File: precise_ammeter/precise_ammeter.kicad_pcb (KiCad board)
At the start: 2 copper layers, 104 parts, among them J1 Conn_01x01_Socket, J2 Conn_01x01_Socket, J3 USB4110GFA, J4 Conn_ARM_JTAG_SWD_10, J5 XT30_Male, J6 Conn_01x04_Socket, U1 INA121U, U10 TPS7A2450DBVR, U11 STM32G431C6Tx, U12 USBLC6-2P6, U2 TLV9301xDBV, U3 TLV9301xDBV, U4 INA137UA, U5 OPA376xxD, U6 OPA376xxD, U7 TPS7A2433DBVR, U8 TPS7A2450DBVR, U9 LMC7660, Y1 Crystal 8MHz

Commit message: layout started
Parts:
- U10, U8: footprint TPS7A2450DBVR:SOT_50DBVR -> TPS7A2433DBVR:SOT23_DBV_TEX
- moved C32 125.6 mm to (233.8, 85.8)
- moved C34 124.4 mm to (235.1, 77.2), turned to 90 degrees
- moved C37 121.1 mm to (231.8, 89.0)
- moved C35 119.6 mm to (228.2, 89.2), turned to 180 degrees
- moved C36 117.9 mm to (228.2, 87.1), turned to 180 degrees
- moved C33 114.5 mm to (225.1, 74.5), turned to 180 degrees
- moved C30 113.9 mm to (222.3, 77.2), turned to 90 degrees
- moved C38 107.2 mm to (216.4, 94.2)
- moved C29 102.2 mm to (213.7, 48.4)
- moved C31 102.2 mm to (213.7, 54.5)
- moved D3 102.2 mm to (237.5, 63.6)
- moved Y1 102.2 mm to (232.5, 50.3)
- moved D4 102.2 mm to (227.9, 55.4)
- moved D5 102.2 mm to (227.9, 58.7)
- moved D6 102.2 mm to (227.9, 62.0)
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
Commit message: USB layout
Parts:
- moved J3 136.7 mm to (246.4, 78.3), turned to 90 degrees
- moved Y1 41.1 mm to (212.1, 86.0), turned to -90 degrees
- moved C31 35.4 mm to (216.1, 89.8), turned to -90 degrees
- moved C29 32.4 mm to (216.0, 80.8), turned to 90 degrees
- moved R25 32.3 mm to (216.1, 86.0), turned to 90 degrees
- moved D4 20.3 mm to (208.1, 50.8)
- moved D5 20.3 mm to (208.1, 54.1)
- moved D7 20.3 mm to (208.1, 60.8)
- moved D6 20.3 mm to (208.1, 57.5)
- moved C38 19.0 mm to (222.3, 76.2), turned to 90 degrees
- moved D3 14.9 mm to (227.0, 53.0)
- moved U12 13.4 mm to (236.7, 78.3)
- moved R1 12.5 mm to (226.3, 60.4)
- moved R5 11.8 mm to (230.4, 60.4)
- moved C37 5.31 mm to (235.7, 85.3), turned to -90 degrees
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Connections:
- U12 pad 1: Net-(U11-PA11) -> Net-(U11-PA12)
- U12 pad 3: Net-(U11-PA12) -> Net-(U11-PA11)
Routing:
- net /MCU/USB_D_N: track 0.00 -> 11.3 mm
- net /MCU/USB_D_P: track 0.00 -> 7.93 mm
- net Net-(U11-PA11): track 0.00 -> 2.81 mm
- net Net-(U11-PA12): track 0.00 -> 2.81 mm

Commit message: idk
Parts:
- moved R28 138.7 mm to (244.8, 72.8), turned to 90 degrees
- moved R29 138.4 mm to (244.8, 84.3), turned to -90 degrees
- moved J5 119.7 mm to (236.5, 94.4)
- moved J6 79.7 mm to (234.0, 65.1), turned to 90 degrees
- moved C1 63.3 mm to (191.2, 77.1)
- moved C5 63.3 mm to (191.2, 80.1)
- moved U7 63.3 mm to (185.9, 78.0)
- moved D6 33.9 mm to (213.0, 91.0)
- moved D7 33.9 mm to (213.0, 94.3)
- moved D5 33.9 mm to (213.0, 87.6)
- moved D4 29.5 mm to (215.4, 79.3), turned to -90 degrees
- moved C31 19.3 mm to (205.6, 73.5), turned to 180 degrees
- moved Y1 16.9 mm to (208.7, 69.4), turned to 180 degrees
- moved D3 15.2 mm to (227.3, 68.2), turned to 90 degrees
- moved R25 13.8 mm to (208.5, 74.4)
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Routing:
- net /MCU/USB_D_P: track 7.93 -> 13.6 mm, vias 0 -> 2
- net Net-(J3-CC2): track 0.00 -> 5.03 mm
- net GND: track 0.00 -> 2.62 mm, vias 0 -> 2
- net /MCU/USB_D_N: track 11.3 -> 13.5 mm
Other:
- board text added: "GND"
- board text added: "SCL"
- board text added: "SDA"
- board text added: "VCC"

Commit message: placement finished
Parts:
- moved R14 100.1 mm to (206.3, 96.7), turned to 90 degrees
- moved R15 96.6 mm to (202.9, 91.7), turned to 180 degrees
- moved R17 95.8 mm to (202.1, 101.7), turned to 90 degrees
- moved C40 93.3 mm to (232.4, 63.4)
- moved D4 91.9 mm to (130.5, 44.0)
- moved D5 91.9 mm to (128.1, 52.3)
- moved D6 91.9 mm to (128.1, 55.6)
- moved D7 91.9 mm to (128.1, 59.0)
- moved C13 90.5 mm to (206.3, 92.3), turned to 90 degrees
- moved C14 87.1 mm to (202.9, 98.1)
- moved C12 84.0 mm to (199.8, 93.3), turned to 90 degrees
- moved C16 82.5 mm to (198.2, 100.6), turned to 90 degrees
- moved R20 82.4 mm to (187.8, 94.5), turned to 90 degrees
- moved R21 80.7 mm to (191.7, 94.6), turned to 90 degrees
- moved R30 80.5 mm to (224.6, 66.5)
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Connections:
- J5 pad 1: VBUS -> GND
- J5 pad 2: GND -> VBUS
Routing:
- net Net-(C31-Pad1): track 0.00 -> 6.98 mm
- net +3V3: track 0.00 -> 5.06 mm
- net Net-(U2--): track 0.00 -> 5.06 mm
- net Net-(U4-IN-): track 0.00 -> 2.84 mm
- net /Curr_measurement/Frontend_2/Stage1_out_2: track 0.00 -> 1.27 mm
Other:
- board text added: "CLK"
- board text added: "DIO"
- board text added: "NRST"
- board text added: "OLED"
- board text added: "SWD"

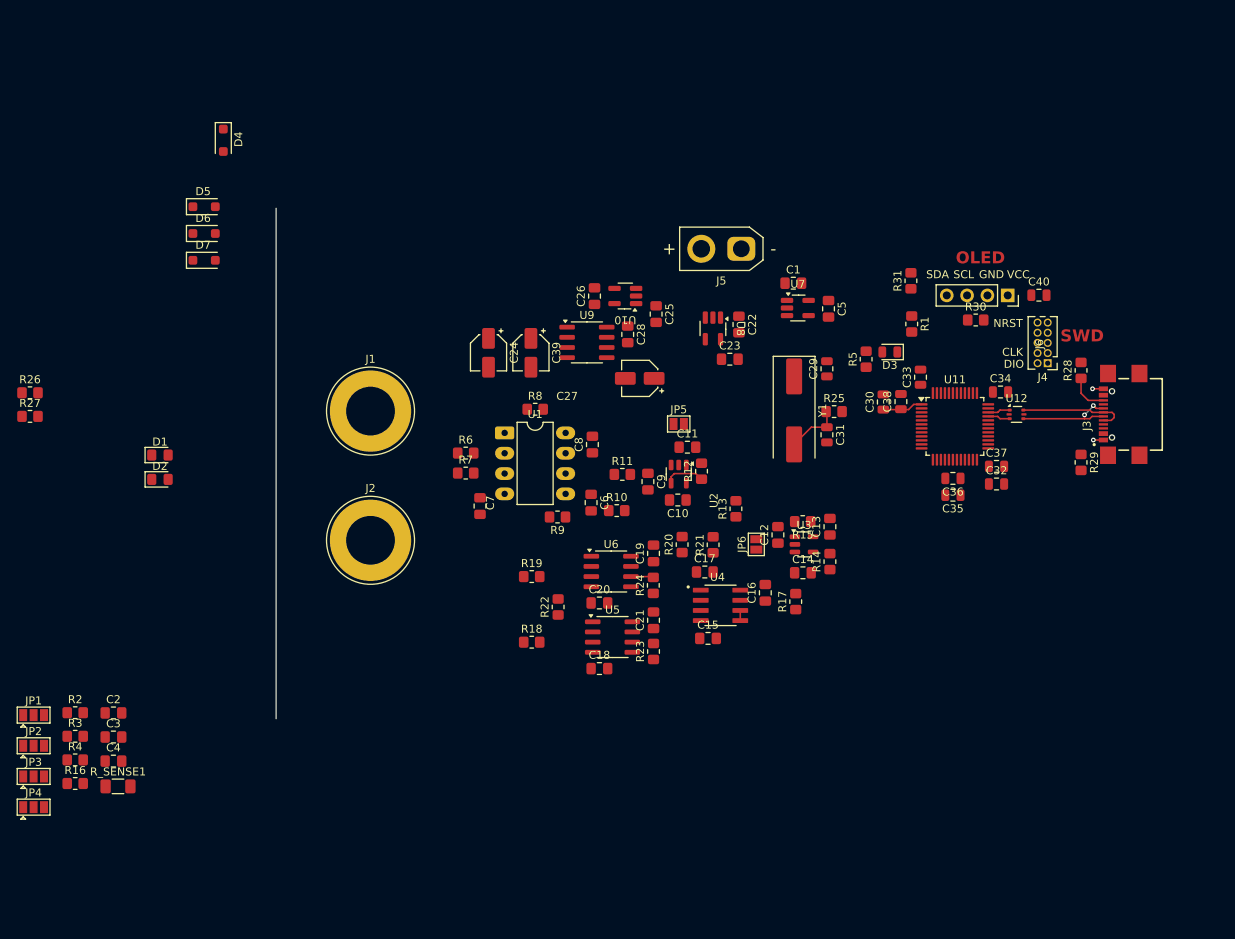
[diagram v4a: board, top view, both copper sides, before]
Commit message: placement changed
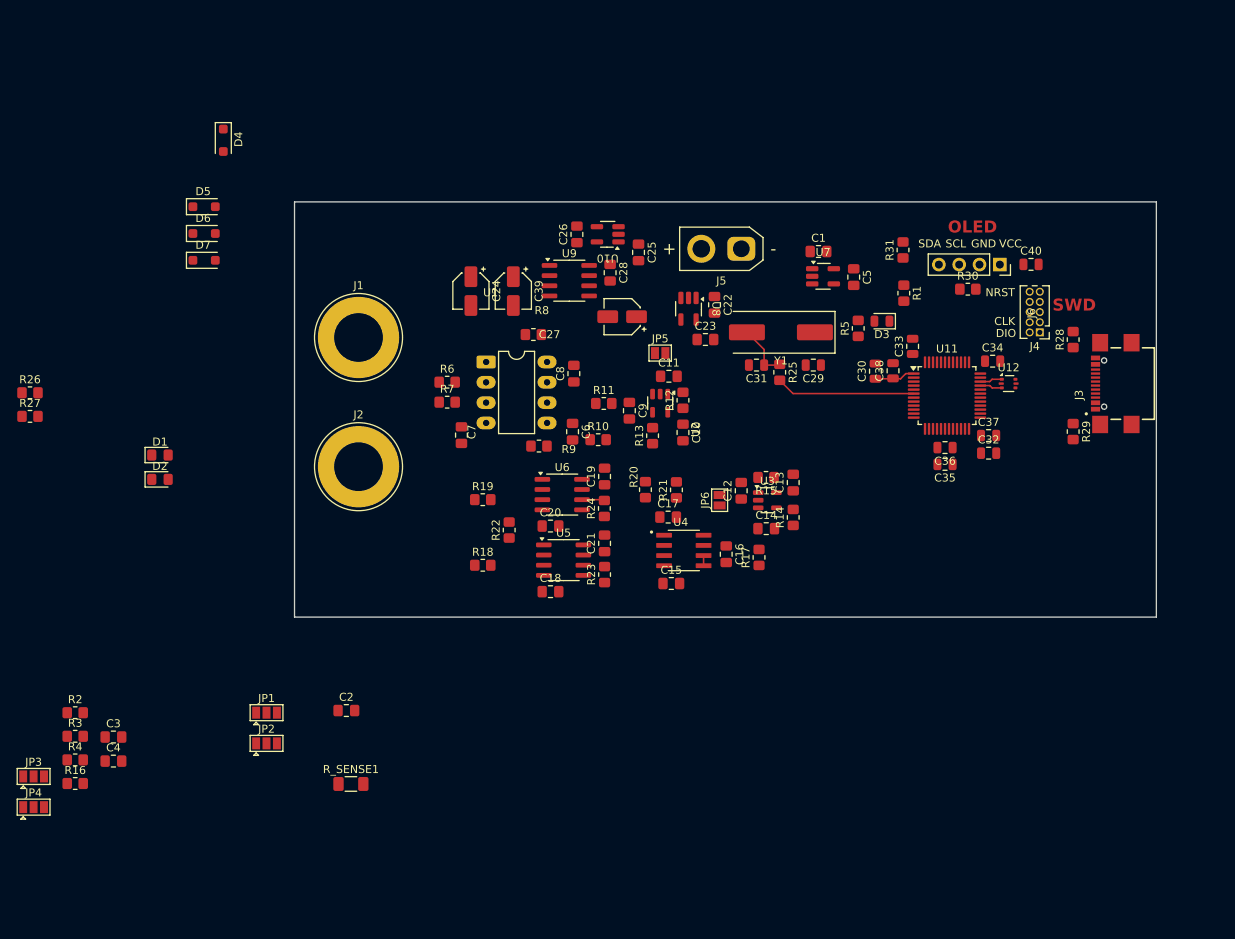
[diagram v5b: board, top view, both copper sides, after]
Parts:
- moved JP1 29.1 mm to (135.9, 115.5)
- moved JP2 29.1 mm to (135.9, 119.4)
- moved C2 29.1 mm to (145.9, 115.3)
- moved R_SENSE1 29.1 mm to (146.4, 124.5)
- moved R13 13.9 mm to (184.2, 80.9)
- moved C31 12.4 mm to (197.2, 72.1), turned to 180 degrees
- moved C19 11.4 mm to (178.2, 86.0)
- moved C21 11.4 mm to (178.2, 94.4)
- moved R24 11.4 mm to (178.1, 90.0)
- moved U6 11.4 mm to (172.9, 88.3)
- moved R18 11.4 mm to (162.9, 97.1)
- moved R19 11.4 mm to (162.9, 88.9)
- moved R22 11.4 mm to (166.2, 92.7)
- moved R23 11.4 mm to (178.2, 98.3)
- moved U5 11.4 mm to (173.0, 96.5)
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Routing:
- net Net-(U11-PF1): track 0.00 -> 17.4 mm
- net /MCU/USB_D_P: track 13.6 -> 0.00 mm, vias 2 -> 0
- net /MCU/USB_D_N: track 13.5 -> 0.00 mm
- net Net-(U2--): track 5.06 -> 0.00 mm
- net Net-(J3-CC2): track 5.03 -> 0.00 mm
- net GND: track 2.62 -> 0.00 mm, vias 2 -> 0
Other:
- board outline added: 107.7 x 51.9 mm

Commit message: jebane gowno
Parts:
- removed C39: 10u, Capacitor_SMD:CP_Elec_4x5.4
- moved R18 91.7 mm to (253.7, 110.3), turned to 90 degrees
- moved JP1 68.1 mm to (201.4, 134.0), turned to 90 degrees
- moved C7 63.1 mm to (216.0, 110.5), turned to 0 degrees
- moved R19 61.7 mm to (205.1, 134.0), turned to 90 degrees
- moved JP3 61.2 mm to (165.2, 105.4)
- moved C13 61.0 mm to (166.9, 136.9), turned to -90 degrees
- moved R14 60.6 mm to (163.4, 138.1)
- moved C19 60.5 mm to (143.1, 135.3)
- moved JP5 60.2 mm to (237.2, 100.7)
- moved C20 59.9 mm to (136.8, 141.1)
- moved R12 59.1 mm to (239.1, 106.2)
- moved R10 59.0 mm to (229.2, 109.7)
- moved C6 59.0 mm to (226.0, 108.7)
- moved R13 59.0 mm to (235.1, 110.7)
- moved C11 59.0 mm to (237.1, 103.2)
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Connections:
- net /Curr_measurement/Analog_out renamed /Analog_IO
- net /Curr_measurement/Stage_1_out renamed /Stage_IO
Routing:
- net Net-(U11-PF1): track 17.4 -> 0.00 mm
- net Net-(C31-Pad1): track 6.98 -> 0.00 mm
- net +3V3: track 5.06 -> 0.00 mm
- net -5VA: track 0.00 -> 3.43 mm
- net Net-(U4-IN-): track 2.84 -> 0.00 mm
- net /Curr_measurement/Frontend_2/Stage1_out_2: track 1.27 -> 0.00 mm
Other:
- board size 107.7 x 51.9 mm -> 71.1 x 73.3 mm
- board text removed: "OLED"

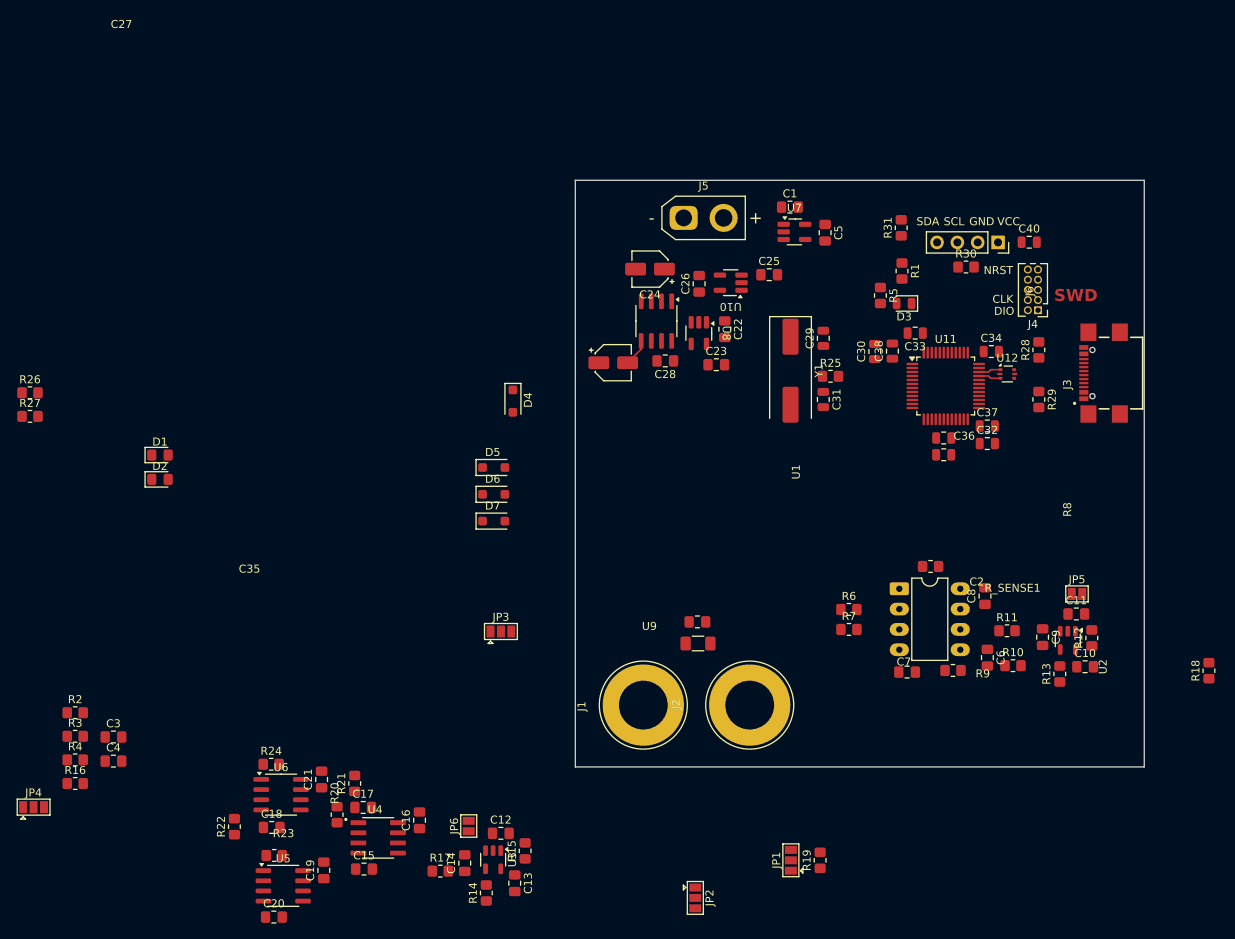
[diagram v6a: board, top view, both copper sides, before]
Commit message: layout almost done. Need to connect Curr_in and fix warnings
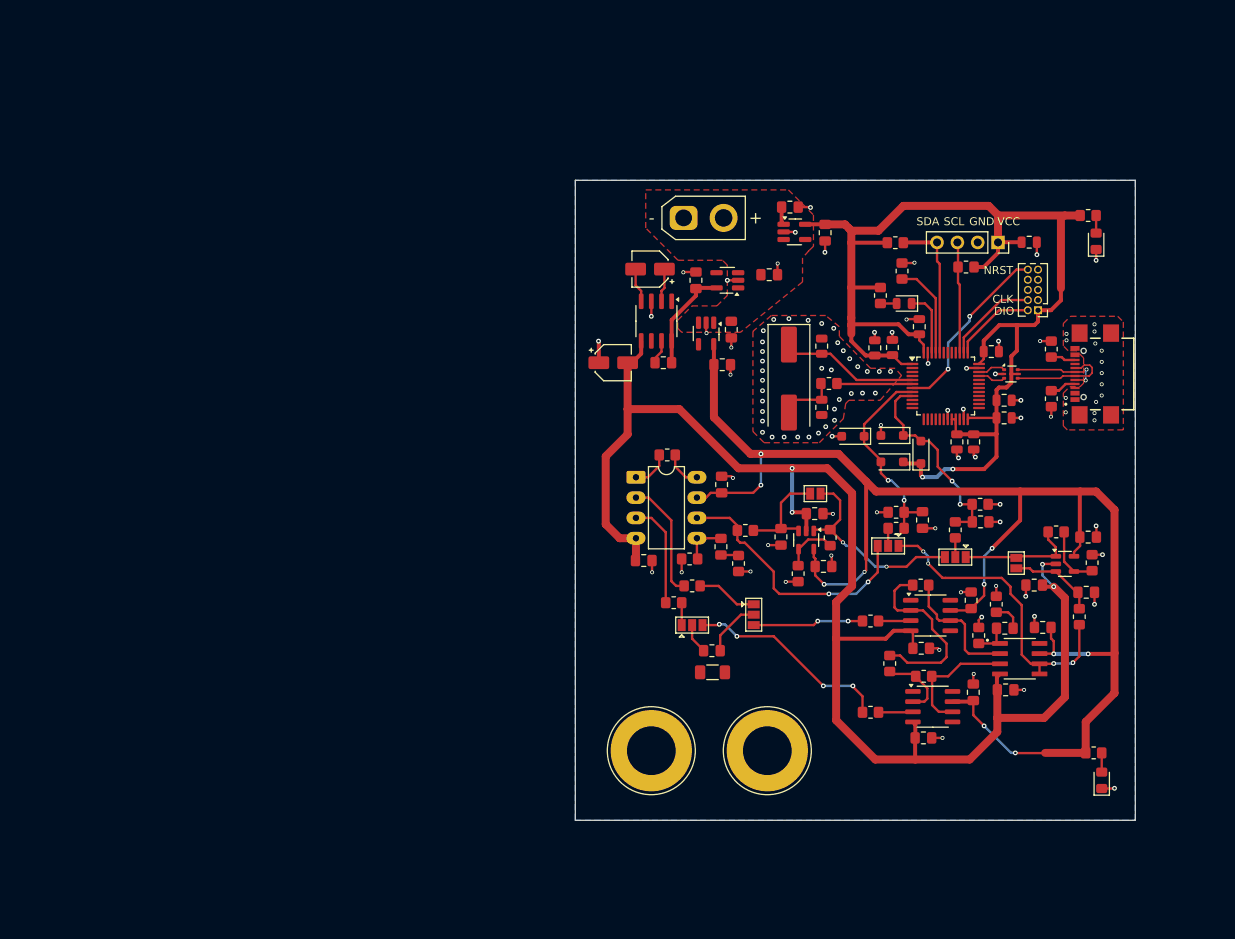
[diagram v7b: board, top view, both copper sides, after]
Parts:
- moved R27 139.5 mm to (239.3, 120.6)
- moved R26 134.1 mm to (238.6, 53.4)
- moved D1 124.5 mm to (240.3, 124.0), turned to 90 degrees
- moved D2 120.7 mm to (239.6, 56.6), turned to 90 degrees
- moved R3 116.8 mm to (225.1, 89.5)
- moved R2 112.4 mm to (222.0, 92.7), turned to -90 degrees
- moved JP4 111.7 mm to (213.6, 94.7), turned to 180 degrees
- moved C3 111.7 mm to (225.2, 91.7)
- moved R16 108.1 mm to (214.6, 90.5), turned to 180 degrees
- moved R4 106.6 mm to (214.6, 92.5), turned to 180 degrees
- moved C4 105.5 mm to (217.9, 91.5), turned to -90 degrees
- moved R14 86.2 mm to (239.1, 96.8), turned to -90 degrees
- moved R17 86.0 mm to (237.5, 103.5), turned to 90 degrees
- moved C14 84.7 mm to (238.4, 100.5), turned to 0 degrees
- moved R22 84.4 mm to (213.8, 109.4)
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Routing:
- net +5VA: track 0.00 -> 192.0 mm, vias 0 -> 10
- net -5VA: track 3.43 -> 181.7 mm, vias 0 -> 4
- net +3V3: track 0.00 -> 162.1 mm, vias 0 -> 2
- net GND: track 0.00 -> 78.4 mm, vias 0 -> 108
- net /Curr_measurement/Frontend_2/Stage1_out_2: track 0.00 -> 39.0 mm, vias 0 -> 4
- net /Curr_measurement/Frontend_1/Stage1_out_1: track 0.00 -> 33.2 mm, vias 0 -> 2
- net /Analog_IO: track 0.00 -> 26.0 mm, vias 0 -> 2
- net /Curr_measurement/Frontend_2/Frontend_2_IN+: track 0.00 -> 25.8 mm, vias 0 -> 4
- net /Curr_measurement/Frontend_1/Frontend_1_OUT: track 0.24 -> 25.8 mm, vias 0 -> 2
- net /Stage_IO: track 0.00 -> 25.3 mm, vias 0 -> 2
- net Net-(U6--): track 0.00 -> 23.2 mm
- net /MCU/NRST: track 0.00 -> 22.8 mm, vias 0 -> 2
- net /MCU/SDA: track 0.00 -> 18.2 mm
- net Net-(U11-PF0): track 0.00 -> 16.7 mm
- net Net-(U4-IN-): track 0.00 -> 16.2 mm
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- added copper zone on B.Cu, net GND
- added copper zone on F.Cu, net GND
- added copper zone on F.Cu, net VBUS
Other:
- board size 71.1 x 73.3 mm -> 70 x 80 mm
- board text removed: "SWD"

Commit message: Layout Done, DRC done
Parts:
- moved R28 0.80 mm to (233.2, 70.1)
- moved R29 0.80 mm to (233.2, 76.3)
- moved J3 0.80 mm to (237.2, 73.2)
- moved JP4 0.41 mm to (213.7, 95.1)
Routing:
- net /Curr_measurement/IN-: track 7.17 -> 10.1 mm
- net /Curr_measurement/IN+: track 3.80 -> 6.68 mm
- net VBUS: track 2.25 -> 0.35 mm
- net /MCU/USB_D_N: track 11.6 -> 10.8 mm
- net /MCU/USB_D_P: track 12.7 -> 11.9 mm
- added copper zone on F.Cu, net /Curr_measurement/IN+
- added copper zone on F.Cu, net /Curr_measurement/IN-
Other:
- board text added: "+3V3"
- board text added: "+5V"
- board text added: "Curr In"
- board text added: "Designed by: Filip Kulka Krzysztof Sikora Dominik Michalczyk"
- board text added: "High res. ammeter"
- board text added: "VBUS"
